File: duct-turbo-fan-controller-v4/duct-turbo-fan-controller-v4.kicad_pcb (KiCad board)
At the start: 2 copper layers, 42.7 x 48.8 mm, 41 parts, among them J1 Screw_Terminal_01x04, J2 Conn_01x04, J3 USB_OTG, J4 AudioJack4, J7 Conn_01x04, Q1 MMBT3904, Q2 BSS84, SW1 SW_Push, SW2 SW_Push, U1 SCD41-D-R2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

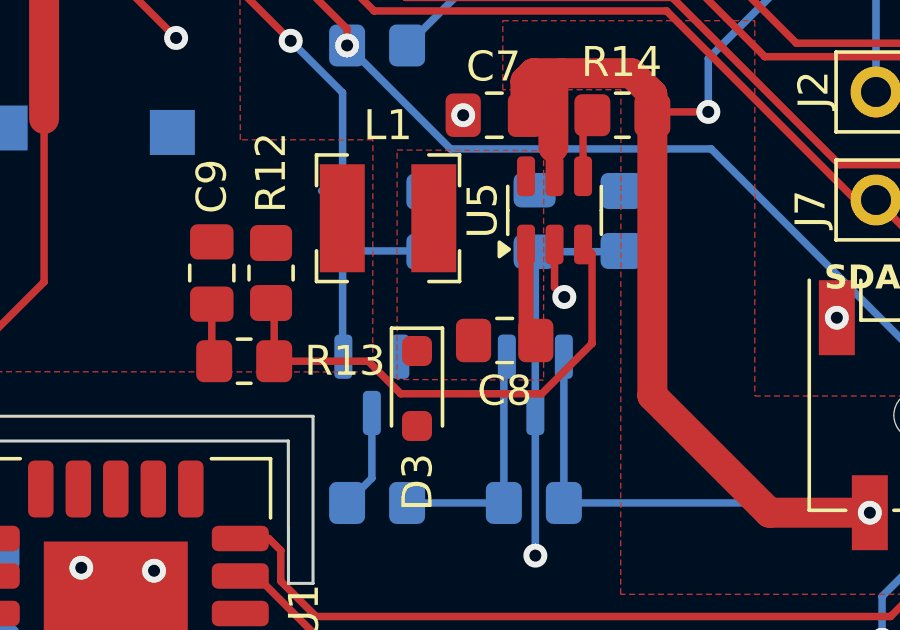
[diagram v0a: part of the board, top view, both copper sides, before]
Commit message: Extra GND vias to help dissipate buck converter thermals
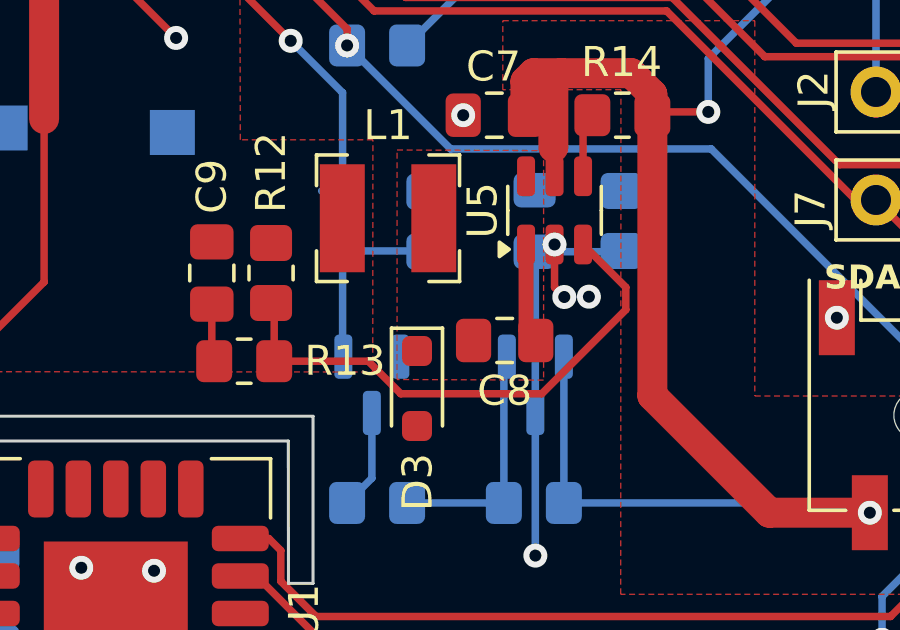
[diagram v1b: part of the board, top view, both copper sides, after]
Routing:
- net Net-(U5-FB): track 17.1 -> 18.1 mm
- net GND: vias 14 -> 16
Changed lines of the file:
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@@
+	)
+	(via
+		(at 94.965 74.56)
+		(size 0.8)
+		(drill 0.4)
+		(layers "F.Cu" "B.Cu")
+		(net 2)
 	)
 	(via
@@
 		(drill 0.4)
 		(layers "F.Cu" "B.Cu")
+		(net 2)
+	)
+	(via
+		(at 96.11 76.3)
+		(size 0.8)
+		(drill 0.4)
+		(layers "F.Cu" "B.Cu")
+		(free yes)
 		(net 2)
 	)
@@
 	)
 	(segment
+		(start 89.84 79.535)
+		(end 94.54 79.535)
+		(width 0.25)
+		(layer "F.Cu")
+		(net 28)
+	)
+	(segment
+		(start 85.62 78.45)
+		(end 88.755 78.45)
+		(width 0.25)
+		(layer "F.Cu")
+		(net 28)
+	)
+	(segment
+		(start 94.54 79.535)
+		(end 97.34 76.735)
+		(width 0.25)
+		(layer "F.Cu")
+		(net 28)
+	)
+	(segment
 		(start 85.62 76.615)
 		(end 85.515 76.51)
@@
 	)
 	(segment
-		(start 89.84 79.535)
-		(end 94.54 79.535)
+		(start 97.34 75.985)
+		(end 95.915 74.56)
 		(width 0.25)
 		(layer "F.Cu")
@@
 	)
 	(segment
-		(start 96.215 77.86)
-		(end 96.215 74.86)
+		(start 88.755 78.45)
+		(end 89.84 79.535)
 		(width 0.25)
 		(layer "F.Cu")
@@
 	)
 	(segment
-		(start 96.215 74.86)
-		(end 95.915 74.56)
-		(width 0.25)
-		(layer "F.Cu")
-		(net 28)
-	)
-	(segment
-		(start 94.54 79.535)
-		(end 96.215 77.86)
-		(width 0.25)
-		(layer "F.Cu")
-		(net 28)
-	)
-	(segment
-		(start 88.755 78.45)
-		(end 85.62 78.45)
-		(width 0.25)
-		(layer "F.Cu")
-		(net 28)
-	)
-	(segment
-		(start 89.84 79.535)
-		(end 88.755 78.45)
-		(width 0.25)
-		(layer "F.Cu")
+		(start 97.34 76.735)
+		(end 97.34 75.985)
+		(width 0.25)
+		(layer "F.Cu")

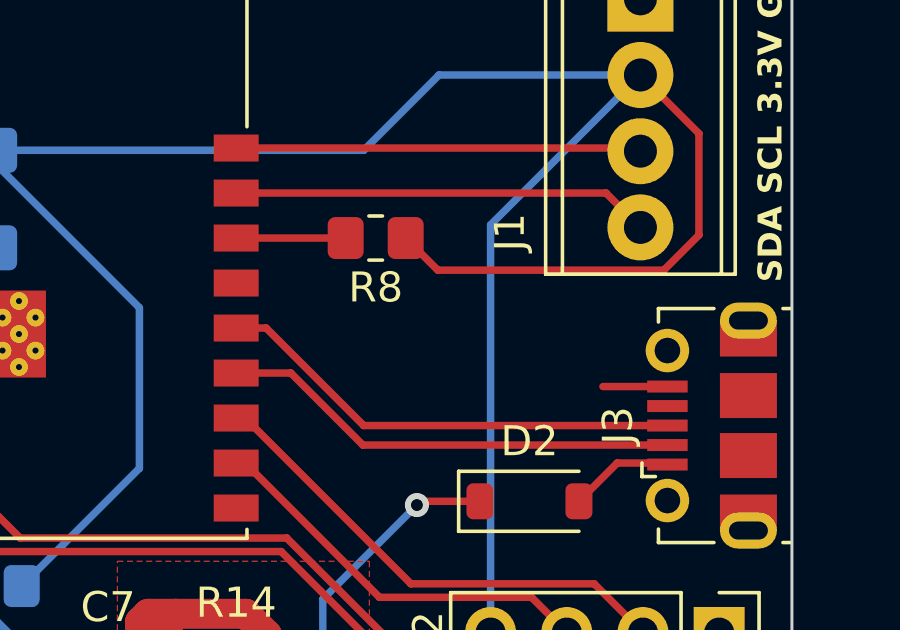
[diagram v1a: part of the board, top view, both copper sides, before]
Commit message: Add LEDs to PCB to help identify state.
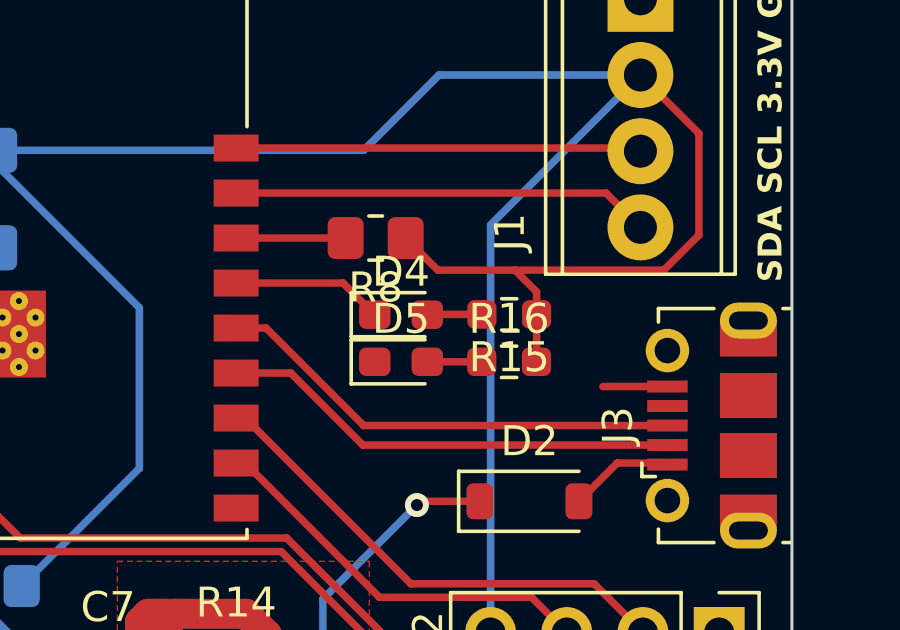
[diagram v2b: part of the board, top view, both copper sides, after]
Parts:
- added D4: LED_Small, LED_SMD:LED_0603_1608Metric_Pad1.05x0.95mm_HandSolder, F.Cu at (102.7, 58.9)
- added D5: LED_Small, LED_SMD:LED_0603_1608Metric_Pad1.05x0.95mm_HandSolder, F.Cu at (102.7, 60.5)
- added R15: R_Small, Resistor_SMD:R_0603_1608Metric_Pad0.98x0.95mm_HandSolder, F.Cu at (106.3, 58.9)
- added R16: R_Small, Resistor_SMD:R_0603_1608Metric_Pad0.98x0.95mm_HandSolder, F.Cu at (106.3, 60.5)
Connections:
- U3 pad 15: unconnected-(U3-IO3-Pad15) -> LED
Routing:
- net LED: track 0.00 -> 5.06 mm
- net +3V3: track 179.5 -> 182.9 mm
- net Net-(D4-A): track 0.00 -> 1.82 mm
- net Net-(D5-A): track 0.00 -> 1.82 mm

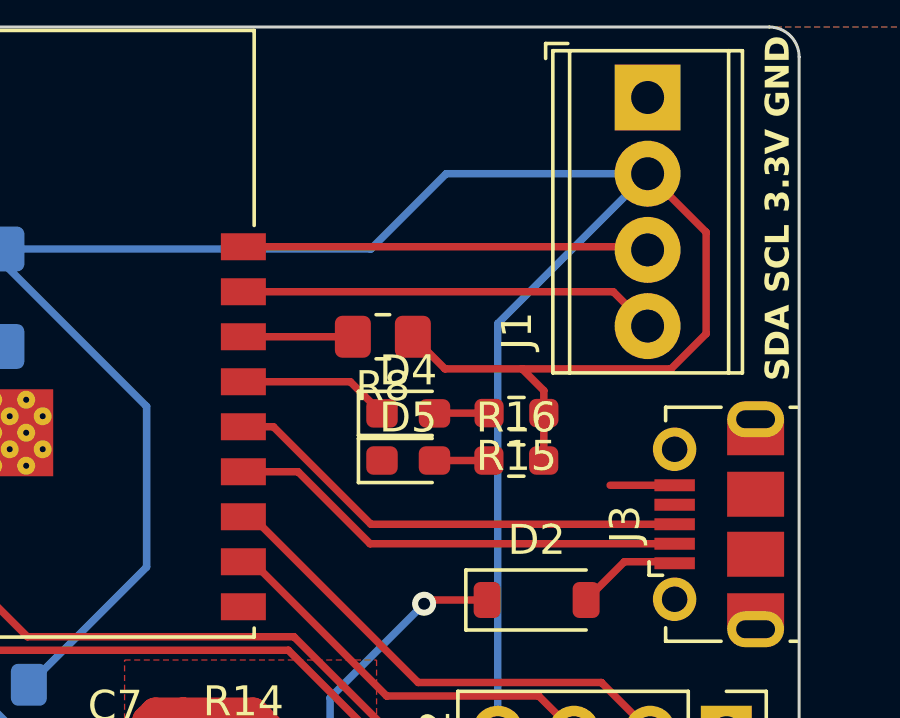
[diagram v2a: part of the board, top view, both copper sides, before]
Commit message: Reduce size of R8 to 0603. Improve labels of LEDs.
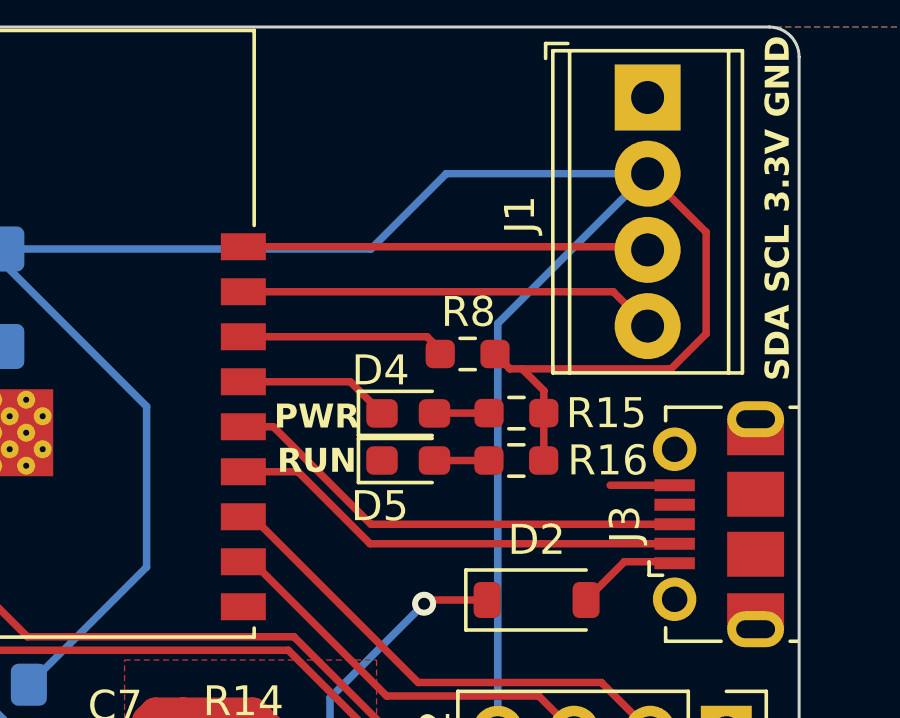
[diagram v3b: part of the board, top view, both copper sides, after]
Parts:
- D2: value D_Small -> PMEG4005EGWX
- D3: value D_Schottky -> PMEG4005EGWX
- R8: footprint Resistor_SMD:R_0805_2012Metric_Pad1.20x1.40mm_HandSolder -> Resistor_SMD:R_0603_1608Metric_Pad0.98x0.95mm_HandSolder
- moved R8 2.88 mm to (104.7, 56.9)
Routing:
- net Net-(U3-IO2): track 3.65 -> 6.88 mm
- net +3V3: track 182.9 -> 179.9 mm
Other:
- board text added: "PWR"
- board text added: "RUN"
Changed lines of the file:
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@@
 		(tags "LED handsolder")
 		(property "Reference" "D4"
-			(at 0 -1.43 0)
+			(at -0.92 -1.43 0)
 			(layer "F.SilkS")
 			(effects
@@
 			)
 		)
-		(property "Datasheet" ""
+		(property "Datasheet" "https://www.bourns.com/docs/Product-Datasheets/SRN4018.pdf"
 			(at 0 0 180)
 			(unlocked yes)
@@
 		(tags "THT Terminal Block Phoenix MPT-0,5-4-2.54 pitch 2.54mm size 10.6x6.2mm^2 drill 1.1mm pad 2.2mm")
 		(property "Reference" "J1"
-			(at 7.78 4.35 90)
+			(at 3.9 4.25 90)
 			(layer "F.SilkS")
 			(effects
@@
 		(tags "LED handsolder")
 		(property "Reference" "D5"
-			(at 0 -1.43 0)
+			(at -0.945 1.525 0)
 			(layer "F.SilkS")
 			(effects
@@
 		(tags "resistor handsolder")
 		(property "Reference" "R15"
-			(at 0 -1.43 360)
+			(at -2.9975 -0.005 0)
 			(layer "F.SilkS")
 			(effects
@@
 		)
 		(property "Value" "R_Small"
-			(at 0 1.43 360)
+			(at 0 1.43 0)
 			(layer "F.Fab")
 			(effects
@@
 		)
 		(fp_text user "${REFERENCE}"
-			(at 0 0 360)
+			(at 0 0 0)
 			(layer "F.Fab")
 			(effects
@@
 		(tags "resistor handsolder")
 		(property "Reference" "R16"
-			(at 0 -1.43 0)
+			(at 3.0525 0 0)
 			(layer "F.SilkS")
 			(effects
@@
 			)
 		)
-		(property "Value" "D_Schottky"
+		(property "Value" "PMEG4005EGWX"
 			(at 0.1 1.9 90)
 			(layer "F.Fab")
@@
 			)
 		)
-		(property "Value" "D_Small"
+		(property "Value" "PMEG4005EGWX"
 			(at 0 2.1 0)
 			(layer "F.Fab")
@@
 		)
 	)
-	(footprint "Resistor_SMD:R_0805_2012Metric_Pad1.20x1.40mm_HandSolder"
+	(footprint "Resistor_SMD:R_0603_1608Metric_Pad0.98x0.95mm_HandSolder"
 		(layer "F.Cu")
-		(at 101.85 56.325 180)
-		(descr "Resistor SMD 0805 (2012 Metric), square (rectangular) end terminal, IPC_7351 nominal with elongated pad for handsoldering. (Body size source: IPC-SM-782 page 72, https://www.pcb-3d.com/wordpress/wp-content/uploads/ipc-sm-782a_amendment_1_and_2.pdf), generated with kicad-footprint-generator")
+		(at 104.675 56.9 180)
+		(descr "Resistor SMD 0603 (1608 Metric), square (rectangular) end terminal, IPC_7351 nominal with elongated pad for handsoldering. (Body size source: IPC-SM-782 page 72, https://www.pcb-3d.com/wordpress/wp-content/uploads/ipc-sm-782a_amendment_1_and_2.pdf), generated with kicad-footprint-generator")
 		(tags "resistor handsolder")
 		(property "Reference" "R8"
-			(at 0 -1.65 0)
+			(at -0.025 1.4 180)
 			(layer "F.SilkS")
 			(effects
@@
 		)
 		(property "Value" "10K"
-			(at 0 1.65 0)
+			(at 0 1.43 180)
 			(layer "F.Fab")
 			(effects
@@
 			)
 		)
-		(property "Footprint" "Resistor_SMD:R_0805_2012Metric_Pad1.20x1.40mm_HandSolder"
+		(property "Footprint" "Resistor_SMD:R_0603_1608Metric_Pad0.98x0.95mm_HandSolder"
 			(at 0 0 180)
 			(unlocked yes)
@@
 		(attr smd)
 		(fp_line
-			(start -0.227064 0.735)
-			(end 0.227064 0.735)
+			(start -0.254724 0.5225)
+			(end 0.254724 0.5225)
 			(stroke
 				(width 0.12)
@@
 		)
 		(fp_line
-			(start -0.227064 -0.735)
-			(end 0.227064 -0.735)
+			(start -0.254724 -0.5225)
+			(end 0.254724 -0.5225)
 			(stroke
 				(width 0.12)
@@
 		)
 		(fp_line
-			(start 1.85 0.95)
-			(end -1.85 0.95)
+			(start 1.65 0.73)
+			(end -1.65 0.73)
 			(stroke
 				(width 0.05)
@@
 		)
 		(fp_line
-			(start 1.85 -0.95)
-			(end 1.85 0.95)
+			(start 1.65 -0.73)
+			(end 1.65 0.73)
 			(stroke
 				(width 0.05)
@@
 		)
 		(fp_line
-			(start -1.85 0.95)
-			(end -1.85 -0.95)
+			(start -1.65 0.73)
+			(end -1.65 -0.73)
 			(stroke
 				(width 0.05)
@@
 		)
 		(fp_line
-			(start -1.85 -0.95)
-			(end 1.85 -0.95)
+			(start -1.65 -0.73)
+			(end 1.65 -0.73)
 			(stroke
 				(width 0.05)
@@
 		)
 		(fp_line
-			(start 1 0.625)
-			(end -1 0.625)
+			(start 0.8 0.4125)
+			(end -0.8 0.4125)
 			(stroke
 				(width 0.1)
@@
 		)
 		(fp_line
-			(start 1 -0.625)
-			(end 1 0.625)
+			(start 0.8 -0.4125)
+			(end 0.8 0.4125)
 			(stroke
 				(width 0.1)
@@
 		)
 		(fp_line
-			(start -1 0.625)
-			(end -1 -0.625)
+			(start -0.8 0.4125)
+			(end -0.8 -0.4125)
 			(stroke
 				(width 0.1)
@@
 		)
 		(fp_line
-			(start -1 -0.625)
-			(end 1 -0.625)
+			(start -0.8 -0.4125)
+			(end 0.8 -0.4125)
 			(stroke
 				(width 0.1)
@@
 		)
 		(fp_text user "${REFERENCE}"
-			(at 0 0 0)
+			(at 0 0 180)
 			(layer "F.Fab")
 			(effects
 				(font
-					(size 0.5 0.5)
-					(thickness 0.08)
+					(size 0.4 0.4)
+					(thickness 0.06)
 				)
 			)
 		)
 		(pad "1" smd roundrect
-			(at -1 0 180)
-			(size 1.2 1.4)
+			(at -0.9125 0 180)
+			(size 0.975 0.95)
 			(layers "F.Cu" "F.Paste" "F.Mask")
-			(roundrect_rratio 0.208333)
+			(roundrect_rratio 0.25)
 			(net 4 "+3V3")
 			(pintype "passive")
 		)
 		(pad "2" smd roundrect
-			(at 1 0 180)
-			(size 1.2 1.4)
+			(at 0.9125 0 180)
+			(size 0.975 0.95)
 			(layers "F.Cu" "F.Paste" "F.Mask")
-			(roundrect_rratio 0.208333)
+			(roundrect_rratio 0.25)
 			(net 24 "Net-(U3-IO2)")
 			(pintype "passive")
 		)
-		(model "${KICAD8_3DMODEL_DIR}/Resistor_SMD.3dshapes/R_0805_2012Metric.wrl"
+		(model "${KICAD8_3DMODEL_DIR}/Resistor_SMD.3dshapes/R_0603_1608Metric.wrl"
 			(offset
 				(xyz 0 0 0)
@@
 		)
 	)
+	(gr_text "RUN"
+		(at 99.65 60.925 0)
+		(layer "F.SilkS")
+		(effects
+			(font
+				(size 0.8 0.8)
+				(thickness 0.2)
+				(bold yes)
+			)
+			(justify bottom)
+		)
+	)
 	(gr_text "SDA SCL 3.3V GND"
 		(at 103.95 76.125 0)
@@
 		)
 	)
+	(gr_text "PWR"
+		(at 99.65 59.45 0)
+		(layer "F.SilkS")
+		(effects
+			(font
+				(size 0.8 0.8)
+				(thickness 0.2)
+				(bold yes)
+			)
+			(justify bottom)
+		)
+	)
 	(segment
 		(start 84.49 85.61)
@@
 	)
 	(segment
+		(start 106.0825 57.395)
+		(end 105.5875 56.9)
+		(width 0.25)
+		(layer "F.Cu")
+		(net 4)
+	)
+	(segment
 		(start 112.625 56.225)
 		(end 112.625 52.84)
@@
 	)
 	(segment
-		(start 103.92 57.395)
-		(end 106.49 57.395)
-		(width 0.25)
-		(layer "F.Cu")
-		(net 4)
-	)
-	(segment
 		(start 75.240001 88.11)
 		(end 73.64 86.509999)
@@
 	)
 	(segment
-		(start 102.85 56.325)
-		(end 103.92 57.395)
-		(width 0.25)
-		(layer "F.Cu")
-		(net 4)
-	)
-	(segment
 		(start 106.49 57.395)
 		(end 111.455 57.395)
@@
 		(net 4)
 	)
+	(segment
+		(start 106.49 57.395)
+		(end 106.0825 57.395)
+		(width 0.25)
+		(layer "F.Cu")
+		(net 4)
+	)
 	(via
 		(at 83.55 53.325)
@@
 	)
 	(segment
+		(start 103.325 56.325)
+		(end 103.7625 56.7625)
+		(width 0.25)
+		(layer "F.Cu")
+		(net 24)
+	)
+	(segment
 		(start 97.2 56.325)
-		(end 100.85 56.325)
+		(end 103.325 56.325)
+		(width 0.25)
+		(layer "F.Cu")
+		(net 24)
+	)
+	(segment
+		(start 103.7625 56.7625)
+		(end 103.7625 56.9)
 		(width 0.25)
 		(layer "F.Cu")

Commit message: Update version number ready for tagging
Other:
- board text added: "Ducturbo/Terra Bloom PWM Fan Controller v4.6"
- board text removed: "Ducturbo/Terra Bloom PWM Fan Controller v4.5"
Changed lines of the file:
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@@
 		)
 	)
-	(gr_text "Ducturbo/Terra Bloom\nPWM Fan Controller v4.5"
+	(gr_text "Ducturbo/Terra Bloom\nPWM Fan Controller v4.6"
 		(at 96.5 91.5 0)
 		(layer "F.SilkS")

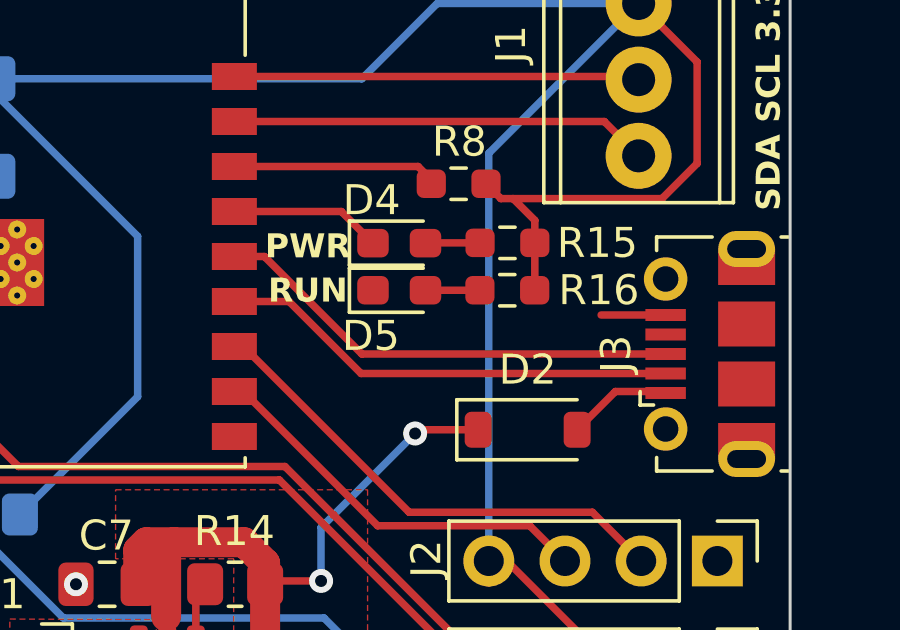
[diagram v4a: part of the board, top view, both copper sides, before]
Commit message: Add values to led resistors. Redraw zone fills.
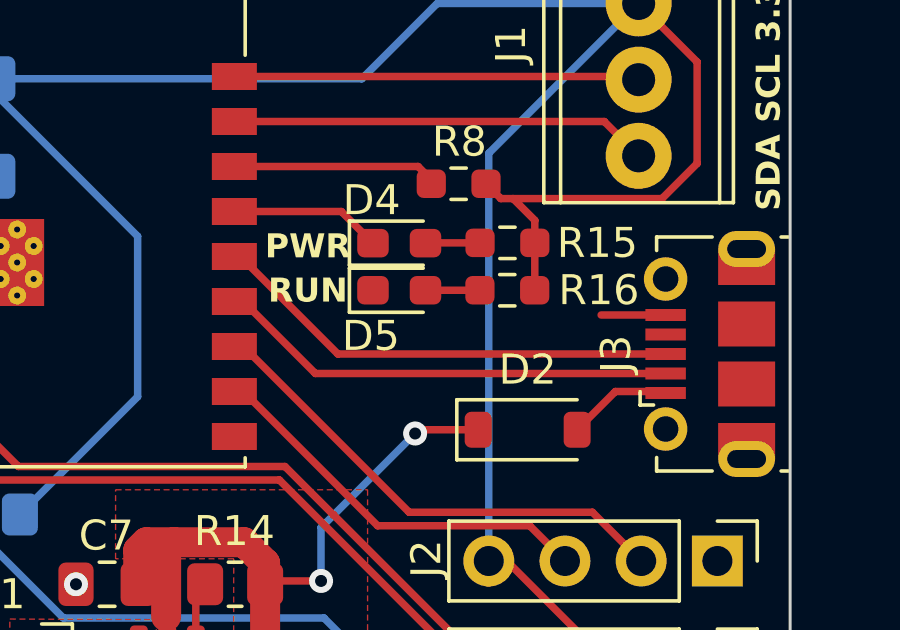
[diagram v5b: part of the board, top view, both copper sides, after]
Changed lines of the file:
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@@
 	(segment
 		(start 97.2 60.825)
-		(end 99.022792 60.825)
+		(end 97.5 60.825)
 		(width 0.25)
 		(layer "F.Cu")
@@
 	)
 	(segment
-		(start 99.022792 60.825)
-		(end 101.422792 63.225)
-		(width 0.25)
-		(layer "F.Cu")
-		(net 14)
-	)
-	(segment
-		(start 101.422792 63.225)
+		(start 99.9 63.225)
 		(end 111.575 63.225)
 		(width 0.25)
@@
 	)
 	(segment
+		(start 97.5 60.825)
+		(end 99.9 63.225)
+		(width 0.25)
+		(layer "F.Cu")
+		(net 14)
+	)
+	(segment
 		(start 97.2 59.325)
-		(end 98.2 59.325)
+		(end 97.4 59.325)
 		(width 0.25)
 		(layer "F.Cu")
@@
 	)
 	(segment
-		(start 98.2 59.325)
-		(end 101.45 62.575)
+		(start 97.4 59.325)
+		(end 100.65 62.575)
 		(width 0.25)
 		(layer "F.Cu")
@@
 	)
 	(segment
-		(start 101.45 62.575)
+		(start 100.65 62.575)
 		(end 111.575 62.575)
 		(width 0.25)
